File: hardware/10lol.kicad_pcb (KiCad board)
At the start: 2 copper layers, 85 parts, among them P1 CONN_2, P2 CONN_2, P3 CONN_4, P4 CONN_4, P5 CONN_3X2, P6 CONN_1, P7 CONN_1, P8 CONN_1, P9 CONN_1, U1 AP1509, U2 ATMEGA328P-P

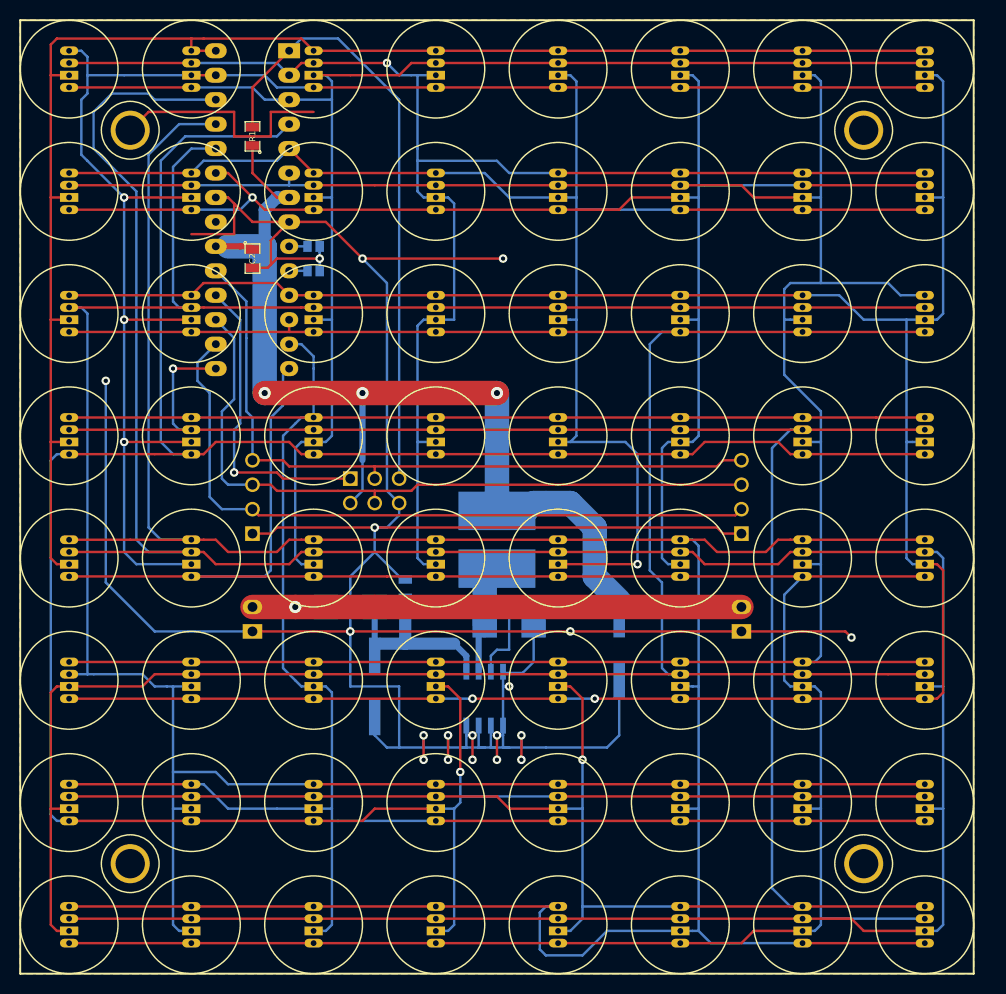
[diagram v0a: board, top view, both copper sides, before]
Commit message: Split out control board.  Simplify LED board.
Signed-off-by: Paul Brook <paul@nowt.org>
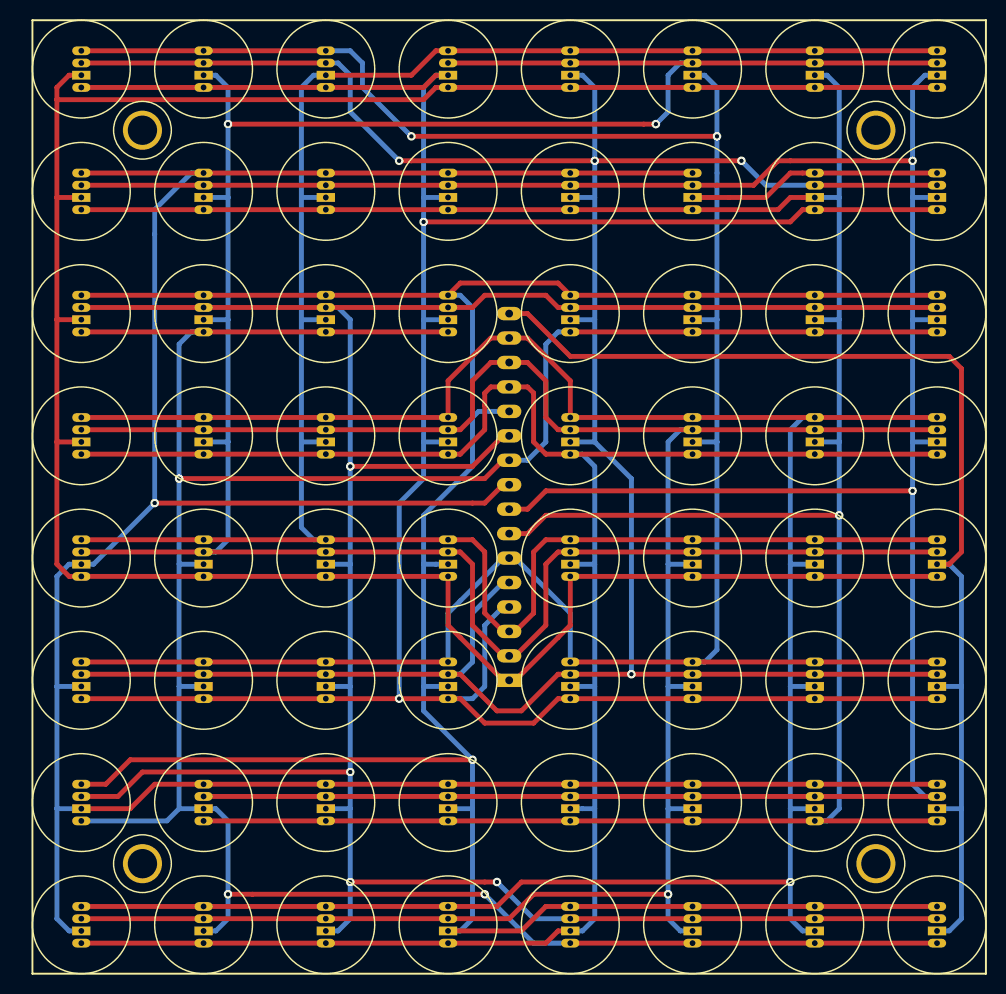
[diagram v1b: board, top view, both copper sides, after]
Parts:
- removed C1: 330u, SMDHD/VF
- removed C2, C4: 100n, SM0805
- removed C3: 100u, SMDHD/VF
- removed D65, D66: DIODESCH, SMB
- removed L1: 39uH, SML88
- removed P6, P7, P8, P9: CONN_1, HOLE3
- removed R1: R, SM0805
- removed R2, R3: 0, SM0603
- removed U1: AP1509, SO8E
- removed U2: ATMEGA328P-P, DIP-28__300_ELL
- P1: value CONN_2 -> CONN_16; footprint PIN_2x1 -> SIL-16-ELL
- P2: value CONN_2 -> CONN_1; footprint PIN_2x1 -> HOLE3; moved to F.Cu
- P3, P4: value CONN_4 -> CONN_1; footprint PIN_ARRAY_4x1 -> HOLE3; moved to F.Cu
- P5: value CONN_3X2 -> CONN_1; footprint pin_array_3x2 -> HOLE3; moved to F.Cu
- moved P5 44.6 mm to (38.1, 37.5)
- moved P4 40.6 mm to (114.3, 37.5), turned to 270 degrees
- moved P3 39.8 mm to (38.1, 113.7), turned to 270 degrees
- moved P1 29.5 mm to (76.2, 75.6)
- moved P2 29.0 mm to (114.3, 113.7), turned to 270 degrees
- moved D57 1.27 mm to (120.7, 31.8)
- moved D58 1.27 mm to (120.7, 44.5)
- moved D59 1.27 mm to (120.7, 57.1)
- moved D60 1.27 mm to (120.7, 69.8)
- moved D61 1.27 mm to (120.7, 82.5)
- moved D62 1.27 mm to (120.7, 95.2)
- moved D63 1.27 mm to (120.7, 108.0)
- moved D64 1.27 mm to (120.7, 120.7)
- moved D10 1.27 mm to (44.5, 44.5)
- moved D11 1.27 mm to (44.5, 57.1)
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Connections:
- D1 pad 1: /C -> /D
- D1 pad 3: /D -> /E
- D1 pad 4: /B -> /F
- D10 pad 1: /F -> /G
- D10 pad 3: /G -> /H
- D10 pad 4: /E -> /J
- D11 pad 1: /J -> /K
- D11 pad 3: /K -> /M
- D11 pad 4: /H -> /N
- D12 pad 1: /N -> /P
- D12 pad 3: /P -> /Q
- D12 pad 4: /M -> /R
- D13 pad 1: /R -> /A
- D13 pad 2: /B -> /K
- D13 pad 3: /S -> /B
- D13 pad 4: /Q -> /C
- D14 pad 1: /H -> /D
- D14 pad 3: /J -> /E
- D14 pad 4: /G -> /F
- D15 pad 1: /N -> /G
- D15 pad 3: /P -> /H
- D15 pad 4: /M -> /J
- D16 pad 1: /R -> /P
- D16 pad 3: /S -> /Q
- D16 pad 4: /Q -> /R
- D17 pad 1: /B -> /D
- D17 pad 3: /D -> /E
- D17 pad 4: /A -> /F
- D18 pad 1: /F -> /G
- D18 pad 3: /G -> /H
- D18 pad 4: /E -> /J
- D19 pad 1: /J -> /K
- D19 pad 3: /K -> /M
- D19 pad 4: /H -> /N
- D2 pad 1: /F -> /G
- D2 pad 3: /G -> /H
- D2 pad 4: /E -> /J
- D20 pad 1: /N -> /P
- D20 pad 3: /P -> /Q
- D20 pad 4: /M -> /R
- D21 pad 1: /R -> /A
- D21 pad 2: /C -> /M
- D21 pad 3: /S -> /B
- D21 pad 4: /Q -> /C
- D22 pad 1: /H -> /D
- D22 pad 3: /J -> /E
- D22 pad 4: /G -> /F
- D23 pad 1: /N -> /G
- D23 pad 3: /P -> /H
- D23 pad 4: /K -> /J
- D24 pad 1: /R -> /P
- D24 pad 3: /S -> /Q
- D24 pad 4: /Q -> /R
- D25 pad 1: /B -> /A
- D25 pad 3: /C -> /B
- D25 pad 4: /A -> /C
- D26 pad 1: /F -> /G
- D26 pad 3: /G -> /H
- D26 pad 4: /E -> /J
- D27 pad 1: /J -> /K
- D27 pad 3: /K -> /M
- D27 pad 4: /H -> /N
- D28 pad 1: /N -> /P
- D28 pad 3: /P -> /Q
- D28 pad 4: /M -> /R
- D29 pad 1: /R -> /A
- D29 pad 2: /D -> /N
- D29 pad 3: /S -> /B
- D29 pad 4: /Q -> /C
- D3 pad 1: /J -> /K
- D3 pad 3: /K -> /M
- D3 pad 4: /H -> /N
- D30 pad 1: /H -> /D
- D30 pad 3: /J -> /E
- D30 pad 4: /G -> /F
- D31 pad 1: /M -> /G
- D31 pad 3: /P -> /H
- D31 pad 4: /K -> /J
- D32 pad 1: /R -> /P
- D32 pad 3: /S -> /Q
- D32 pad 4: /Q -> /R
- D33 pad 1: /B -> /A
- D33 pad 3: /C -> /B
- D33 pad 4: /A -> /C
- D34 pad 1: /F -> /G
- D34 pad 3: /G -> /H
- D34 pad 4: /D -> /J
- D35 pad 1: /J -> /K
- D35 pad 3: /K -> /M
- D35 pad 4: /H -> /N
- D36 pad 1: /N -> /P
- D36 pad 3: /P -> /Q
- D36 pad 4: /M -> /R
- D37 pad 1: /R -> /A
- D37 pad 2: /E -> /P
- D37 pad 3: /S -> /B
- D37 pad 4: /Q -> /C
- D38 pad 1: /H -> /D
- D38 pad 3: /J -> /E
- D38 pad 4: /G -> /F
- D39 pad 1: /M -> /G
- D39 pad 3: /N -> /H
- D39 pad 4: /K -> /J
- D4 pad 1: /N -> /P
- D4 pad 3: /P -> /Q
- D4 pad 4: /M -> /R
- D40 pad 1: /R -> /K
- D40 pad 3: /S -> /M
- D40 pad 4: /Q -> /N
- D41 pad 1: /B -> /A
- D41 pad 3: /C -> /B
- D41 pad 4: /A -> /C
- D42 pad 1: /E -> /G
- D42 pad 3: /G -> /H
- D42 pad 4: /D -> /J
- D43 pad 1: /J -> /K
- D43 pad 3: /K -> /M
- D43 pad 4: /H -> /N
- D44 pad 1: /N -> /P
- D44 pad 3: /P -> /Q
- D44 pad 4: /M -> /R
- D45 pad 1: /R -> /A
- D45 pad 2: /F -> /Q
- D45 pad 3: /S -> /B
- D45 pad 4: /Q -> /C
- D46 pad 1: /H -> /D
- D46 pad 3: /J -> /E
- D46 pad 4: /G -> /F
- D47 pad 1: /M -> /G
- D47 pad 3: /N -> /H
- D47 pad 4: /K -> /J
- D48 pad 1: /R -> /K
- D48 pad 3: /S -> /M
- D48 pad 4: /P -> /N
- D49 pad 1: /B -> /A
- D49 pad 3: /C -> /B
- D49 pad 4: /A -> /C
- D5 pad 1: /R -> /A
- D5 pad 2: /A -> /J
- D5 pad 3: /S -> /B
- D5 pad 4: /Q -> /C
- D50 pad 1: /E -> /D
- D50 pad 3: /F -> /E
- D50 pad 4: /D -> /F
- D51 pad 1: /J -> /K
- D51 pad 3: /K -> /M
- D51 pad 4: /H -> /N
- D52 pad 1: /N -> /P
- D52 pad 3: /P -> /Q
- D52 pad 4: /M -> /R
- D53 pad 1: /R -> /A
- D53 pad 2: /G -> /R
- D53 pad 3: /S -> /B
- D53 pad 4: /Q -> /C
- D54 pad 1: /H -> /D
- D54 pad 3: /J -> /E
- D54 pad 4: /G -> /F
- D55 pad 1: /M -> /G
- D55 pad 3: /N -> /H
- D55 pad 4: /K -> /J
- D56 pad 1: /Q -> /K
- D56 pad 3: /S -> /M
- D56 pad 4: /P -> /N
- D57 pad 1: /B -> /A
- D57 pad 3: /C -> /B
- D57 pad 4: /A -> /C
- D58 pad 1: /E -> /D
- D58 pad 3: /F -> /E
- D58 pad 4: /D -> /F
- D59 pad 1: /J -> /K
- D59 pad 3: /K -> /M
- D59 pad 4: /G -> /N
- D6 pad 1: /H -> /D
- D6 pad 3: /K -> /E
- D6 pad 4: /G -> /F
- D60 pad 1: /N -> /P
- D60 pad 3: /P -> /Q
- D60 pad 4: /M -> /R
- D61 pad 1: /R -> /A
- D61 pad 2: /H -> /S
- D61 pad 3: /S -> /B
- D61 pad 4: /Q -> /C
- D62 pad 1: /H -> /D
- D62 pad 3: /J -> /E
- D62 pad 4: /G -> /F
- D63 pad 1: /M -> /G
- D63 pad 3: /N -> /H
- D63 pad 4: /K -> /J
- D64 pad 1: /Q -> /K
- D64 pad 3: /R -> /M
- D64 pad 4: /P -> /N
- D7 pad 1: /N -> /K
- D7 pad 3: /P -> /M
- D7 pad 4: /M -> /N
- D8 pad 1: /R -> /P
- D8 pad 3: /S -> /Q
- D8 pad 4: /Q -> /R
- D9 pad 1: /C -> /D
- D9 pad 3: /D -> /E
- D9 pad 4: /A -> /F
- P1 pad 1: /GND -> /A
- P1 pad 2: /raw -> /B
- P2 pad 1: /GND -> (no net)
- P3 pad 1: /GND -> (no net)
- P4 pad 1: /GND -> (no net)
- P5 pad 1: /MISO -> (no net)
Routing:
- net /GND: track 374.4 -> 0.00 mm, vias 19 -> 0
- net /S: track 293.0 -> 118.2 mm
- net /5v: track 129.8 -> 0.00 mm, vias 3 -> 0
- net /F: track 154.2 -> 273.6 mm, vias 1 -> 2
- net /D: track 153.7 -> 272.7 mm, vias 1 -> 2
- net /E: track 162.3 -> 274.9 mm, vias 1 -> 4
- net /A: track 158.5 -> 259.0 mm
- net /B: track 171.7 -> 269.9 mm, vias 3 -> 2
- net /C: track 152.6 -> 228.3 mm
- net /DATA: track 73.9 -> 0.00 mm
- net /SCK: track 73.9 -> 0.00 mm
- net /CS: track 73.5 -> 0.00 mm
- net /RESET: track 63.5 -> 0.00 mm
- net /Q: track 287.6 -> 224.4 mm, vias 0 -> 1
- net /P: track 273.3 -> 212.0 mm, vias 2 -> 0
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- removed copper zone on B.Cu, net /GND
- removed copper zone on F.Cu, net /GND
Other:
- net class Default: trace_width 0.254 -> 0.508
- net class Power removed
- board text removed: "+"
- board text removed: "-"
- board text removed: "CS"
- board text removed: "DATA"
- board text removed: "GND"
- board text removed: "SCK"
- board text removed: "a0"
- board text removed: "a1"

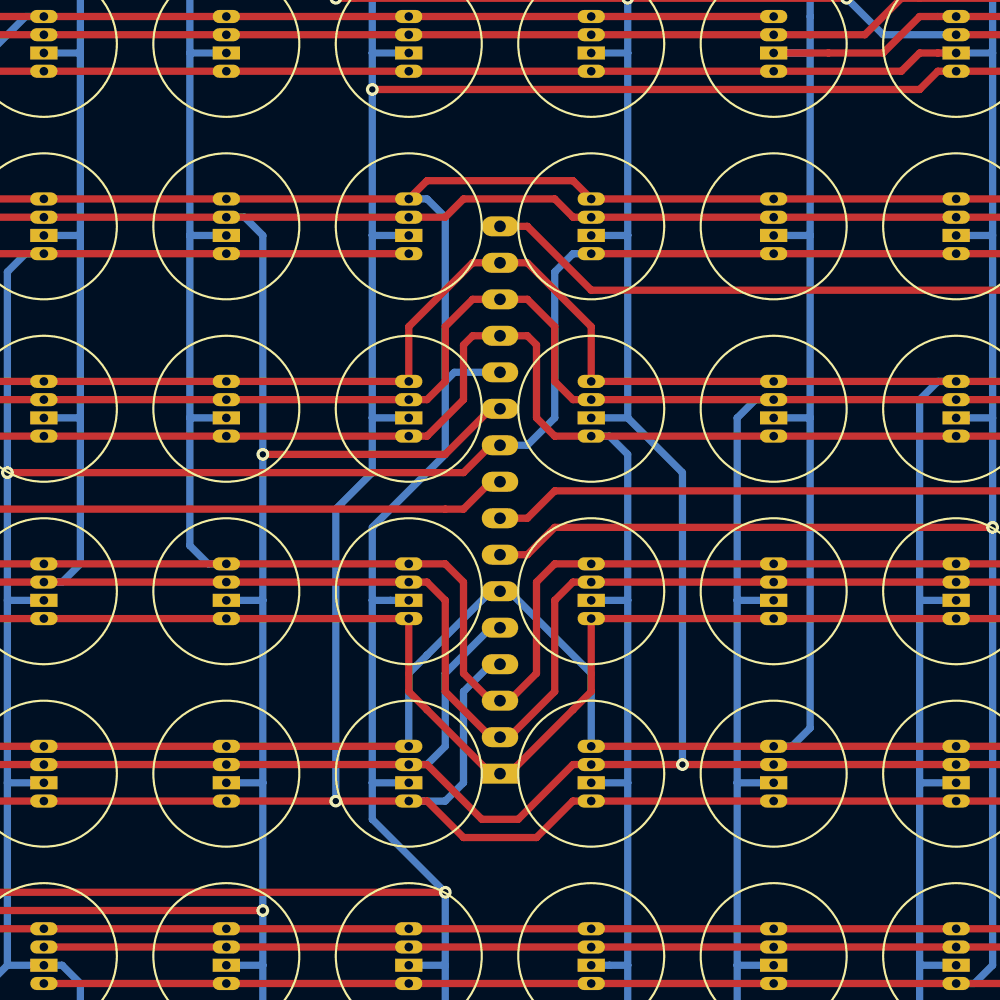
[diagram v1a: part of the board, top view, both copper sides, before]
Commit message: Create control board PCB.  Finish LED board layout.
Signed-off-by: Paul Brook <paul@nowt.org>
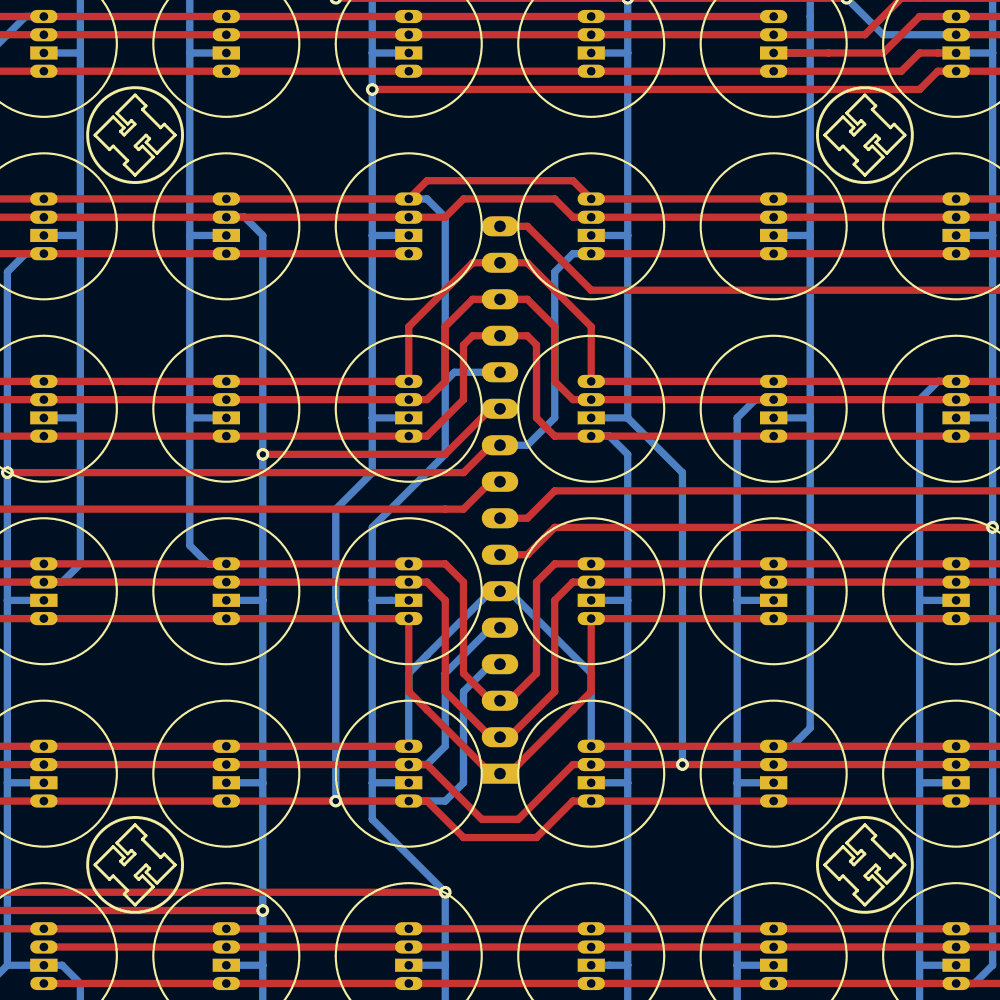
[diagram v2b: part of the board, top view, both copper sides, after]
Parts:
- added G***: OSHW_LOGO, OSHW_LOGO, B.Cu at (88.9, 49.5)
- added HACKSPACE_LOGO: VAL**, HACKSPACE_LOGO, B.Cu at (62.9, 43.8)
- added LOGO_SMALL1: LOGO_S1, LOGO_SMALL, F.Cu at (50.8, 50.2)
- added LOGO_SMALL2: LOGO_S2, LOGO_SMALL, F.Cu at (50.8, 101.0)
- added LOGO_SMALL3: LOGO_S3, LOGO_SMALL, F.Cu at (101.6, 101.0)
- added LOGO_SMALL4: LOGO_S4, LOGO_SMALL, F.Cu at (101.6, 50.2)
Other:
- board text added: "CONTROL BOARD HERE"
- board text added: "©Paul Brook"
